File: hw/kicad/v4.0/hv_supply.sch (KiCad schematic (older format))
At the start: 32 parts, among them U4 ACT4088, U5 LNK304D

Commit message: Added LCSC # to parts in 4.3 PCB
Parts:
- C145, C35, C4, C51, C68, C69, C70, C97: LCSC (none) -> C15850
- C15, C41, C58, C60: LCSC (none) -> C14663
- C50: LCSC (none) -> C23630
- D10, D11: LCSC (none) -> C86560
- D6: LCSC (none) -> C8678
- D8: LCSC (none) -> C2297
- R143: LCSC (none) -> C22843
- R15, R16, R30, R75, R91: LCSC (none) -> C21190
- R161: LCSC (none) -> C23018
- R19, R92: LCSC (none) -> C22809
- R21: LCSC (none) -> C23196
- U4: LCSC (none) -> C11135
- U5: LCSC (none) -> C37448
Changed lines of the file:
@@
 EESchema Schematic File Version 4
 LIBS:stmbl_4.0-cache
-EELAYER 26 0
+EELAYER 30 0
 EELAYER END
 $Descr A4 11693 8268
@@
 F 9 "" H 0   0   50  0001 C CNN "Description"
 F 10 "Micro Commercial Co" H 0   0   50  0001 C CNN "Manufacturer"
+F 11 "C86560" H 6400 4250 50  0001 C CNN "LCSC"
 	1    6400 4250
 	0    1    1    0
@@
 F 9 "" H 0   0   50  0001 C CNN "Description"
 F 10 "Micro Commercial Co" H 0   0   50  0001 C CNN "Manufacturer"
+F 11 "C86560" H 7200 3750 50  0001 C CNN "LCSC"
 	1    7200 3750
 	0    1    1    0
@@
 F 9 "" H 0   0   50  0001 C CNN "Description"
 F 10 "" H 0   0   50  0001 C CNN "Manufacturer"
+F 11 " C14663" H 7200 4250 50  0001 C CNN "LCSC"
 	1    7200 4250
 	1    0    0    -1
@@
 F 9 "" H 0   0   50  0001 C CNN "Description"
 F 10 "" H 0   0   50  0001 C CNN "Manufacturer"
+F 11 " C15850" H 6400 3750 50  0001 C CNN "LCSC"
 	1    6400 3750
 	1    0    0    -1
@@
 F 9 "" H 0   0   50  0001 C CNN "Description"
 F 10 "" H 0   0   50  0001 C CNN "Manufacturer"
+F 11 " C14663" H 5250 3750 50  0001 C CNN "LCSC"
 	1    5250 3750
 	1    0    0    -1
@@
 F 9 "" H 0   0   50  0001 C CNN "Description"
 F 10 "" H 0   0   50  0001 C CNN "Manufacturer"
+F 11 "C21190" H 5600 3750 50  0001 C CNN "LCSC"
 	1    5600 3750
 	-1   0    0    1
@@
 F 9 "" H 0   0   50  0001 C CNN "Description"
 F 10 "" H 0   0   50  0001 C CNN "Manufacturer"
+F 11 "C22809" H 6550 3100 50  0001 C CNN "LCSC"
 	1    6550 3100
 	0    -1   -1   0
@@
 F 9 "" H 0   0   50  0001 C CNN "Description"
 F 10 "Lite-On" H 0   0   50  0001 C CNN "Manufacturer"
+F 11 "C2297" H 9300 4350 50  0001 C CNN "LCSC"
 	1    9300 4350
 	0    -1   -1   0
@@
 F 9 "" H 0   0   50  0001 C CNN "Description"
 F 10 "" H 0   0   50  0001 C CNN "Manufacturer"
+F 11 "C21190" H 9300 3900 50  0001 C CNN "LCSC"
 	1    9300 3900
 	1    0    0    -1
@@
 F 9 "" H 0   0   50  0001 C CNN "Description"
 F 10 "" H 0   0   50  0001 C CNN "Manufacturer"
+F 11 "C23196" H 2700 6200 50  0001 C CNN "LCSC"
 	1    2700 6200
 	0    1    1    0
@@
 F 9 "" H 0   0   50  0001 C CNN "Description"
 F 10 "" H 0   0   50  0001 C CNN "Manufacturer"
+F 11 "C22809" H 2450 6450 50  0001 C CNN "LCSC"
 	1    2450 6450
 	1    0    0    -1
@@
 F 9 "" H 0   0   50  0001 C CNN "Description"
 F 10 "Multicomp" H 0   0   50  0001 C CNN "Manufacturer"
+F 11 "C8678" H 2950 6850 50  0001 C CNN "LCSC"
 	1    2950 6850
 	0    1    1    0
@@
 F 9 "" H 0   0   50  0001 C CNN "Description"
 F 10 "" H 0   0   50  0001 C CNN "Manufacturer"
+F 11 " C14663" H 2600 5900 50  0001 C CNN "LCSC"
 	1    2600 5900
 	0    -1   -1   0
@@
 F 9 "" H 0   0   50  0001 C CNN "Description"
 F 10 "Active-Semi" H 0   0   50  0001 C CNN "Manufacturer"
+F 11 "C11135" H 1950 6050 50  0001 C CNN "LCSC"
 	1    1950 6050
 	1    0    0    -1
@@
 F 9 "" H 0   0   50  0001 C CNN "Description"
 F 10 "" H 0   0   50  0001 C CNN "Manufacturer"
+F 11 "C21190" H 9300 3500 50  0001 C CNN "LCSC"
 	1    9300 3500
 	1    0    0    -1
@@
 F 9 "" H 0   0   50  0001 C CNN "Description"
 F 10 "" H 0   0   50  0001 C CNN "Manufacturer"
+F 11 " C15850" H 3750 6450 50  0001 C CNN "LCSC"
 	1    3750 6450
 	1    0    0    -1
@@
 F 9 "" H 0   0   50  0001 C CNN "Description"
 F 10 "" H 0   0   50  0001 C CNN "Manufacturer"
+F 11 " C14663" H 3250 6450 50  0001 C CNN "LCSC"
 	1    3250 6450
 	1    0    0    -1
@@
 F 9 "" H 0   0   50  0001 C CNN "Description"
 F 10 "Power Integrations" H 0   0   50  0001 C CNN "Manufacturer"
+F 11 "C37448" H 4600 3600 50  0001 C CNN "LCSC"
 	1    4600 3600
 	1    0    0    -1
@@
 F 9 "" H 0   0   50  0001 C CNN "Description"
 F 10 "" H 0   0   50  0001 C CNN "Manufacturer"
+F 11 "C21190" H 2450 6850 50  0001 C CNN "LCSC"
 	1    2450 6850
 	1    0    0    -1
@@
 F 9 "" H 0   0   50  0001 C CNN "Description"
 F 10 "" H 0   0   50  0001 C CNN "Manufacturer"
+F 11 "C21190" H 5600 3350 50  0001 C CNN "LCSC"
 	1    5600 3350
 	-1   0    0    1
@@
 F 9 "" H 0   0   50  0001 C CNN "Description"
 F 10 "" H 0   0   50  0001 C CNN "Manufacturer"
+F 11 "C22843" H 6150 3100 50  0001 C CNN "LCSC"
 	1    6150 3100
 	0    -1   -1   0
@@
 F 9 "" H 0   0   50  0001 C CNN "Description"
 F 10 "" H 0   0   50  0001 C CNN "Manufacturer"
+F 11 "C23630" H 3500 6450 50  0001 C CNN "LCSC"
 	1    3500 6450
 	1    0    0    -1
@@
 F 9 "" H 0   0   50  0001 C CNN "Description"
 F 10 "" H 0   0   50  0001 C CNN "Manufacturer"
+F 11 " C15850" H 7950 4250 50  0001 C CNN "LCSC"
 	1    7950 4250
 	1    0    0    -1
@@
 F 9 "" H 0   0   50  0001 C CNN "Description"
 F 10 "" H 0   0   50  0001 C CNN "Manufacturer"
+F 11 " C15850" H 7450 4250 50  0001 C CNN "LCSC"
 	1    7450 4250
 	1    0    0    -1
@@
 F 9 "" H 0   0   50  0001 C CNN "Description"
 F 10 "" H 0   0   50  0001 C CNN "Manufacturer"
+F 11 " C15850" H 4000 6450 50  0001 C CNN "LCSC"
 	1    4000 6450
 	1    0    0    -1
@@
 F 9 "" H 0   0   50  0001 C CNN "Description"
 F 10 "" H 0   0   50  0001 C CNN "Manufacturer"
+F 11 "C23018" H 8700 4250 50  0001 C CNN "LCSC"
 	1    8700 4250
 	1    0    0    -1
@@
 F 9 "" H 0   0   50  0001 C CNN "Description"
 F 10 "" H 0   0   50  0001 C CNN "Manufacturer"
+F 11 " C15850" H 7700 4250 50  0001 C CNN "LCSC"
 	1    7700 4250
 	1    0    0    -1
@@
 F 9 "" H 0   0   50  0001 C CNN "Description"
 F 10 "" H 0   0   50  0001 C CNN "Manufacturer"
+F 11 " C15850" H 8200 4250 50  0001 C CNN "LCSC"
 	1    8200 4250
 	1    0    0    -1
@@
 F 9 "" H 0   0   50  0001 C CNN "Description"
 F 10 "" H 0   0   50  0001 C CNN "Manufacturer"
+F 11 " C15850" H 8450 4250 50  0001 C CNN "LCSC"
 	1    8450 4250
 	1    0    0    -1

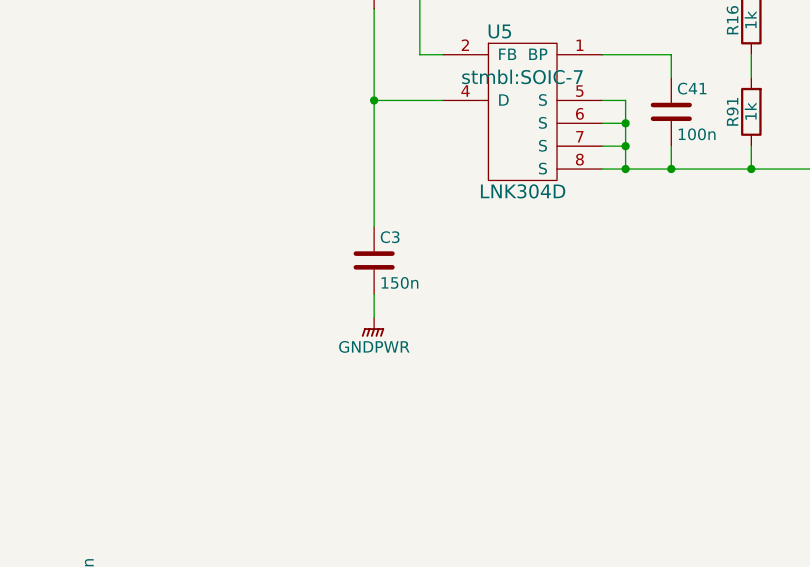
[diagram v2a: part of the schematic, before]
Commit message: Changed 120uf 1808 to 1210 100uF
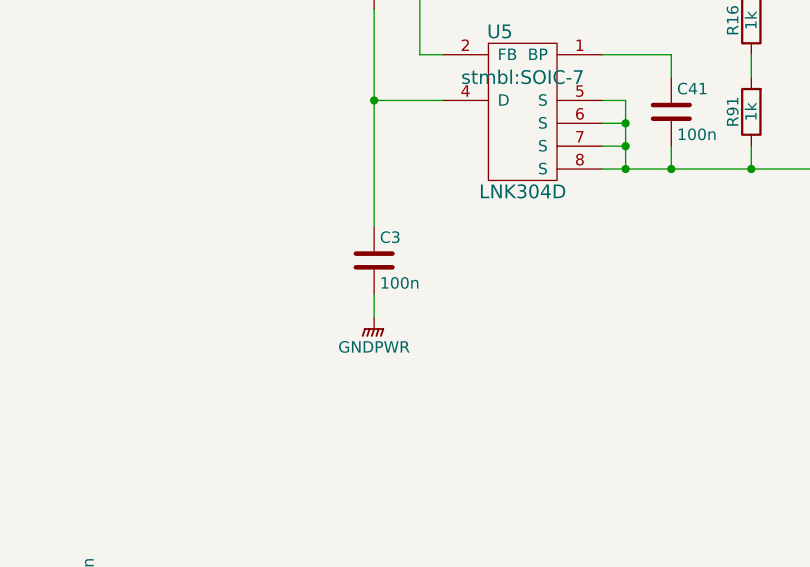
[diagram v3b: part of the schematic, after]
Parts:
- C145, C35, C4, C51, C68, C69, C70, C97: LCSC C15850 -> C15850
- C15, C41, C58, C60: LCSC C14663 -> C14663
- C3: value 150n -> 100n; footprint stmbl:C_1808 -> Capacitor_SMD:C_1210_3225Metric; LCSC (none) -> C141218; Manufacturer No C1808W154KCRACTU -> C1210C104KCRAC7800
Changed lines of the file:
@@
 F 9 "" H 0   0   50  0001 C CNN "Description"
 F 10 "" H 0   0   50  0001 C CNN "Manufacturer"
-F 11 " C14663" H 7200 4250 50  0001 C CNN "LCSC"
+F 11 "C14663" H 7200 4250 50  0001 C CNN "LCSC"
 	1    7200 4250
 	1    0    0    -1
@@
 F 9 "" H 0   0   50  0001 C CNN "Description"
 F 10 "" H 0   0   50  0001 C CNN "Manufacturer"
-F 11 " C15850" H 6400 3750 50  0001 C CNN "LCSC"
+F 11 "C15850" H 6400 3750 50  0001 C CNN "LCSC"
 	1    6400 3750
 	1    0    0    -1
@@
 F 9 "" H 0   0   50  0001 C CNN "Description"
 F 10 "" H 0   0   50  0001 C CNN "Manufacturer"
-F 11 " C14663" H 5250 3750 50  0001 C CNN "LCSC"
+F 11 "C14663" H 5250 3750 50  0001 C CNN "LCSC"
 	1    5250 3750
 	1    0    0    -1
@@
 F 9 "" H 0   0   50  0001 C CNN "Description"
 F 10 "" H 0   0   50  0001 C CNN "Manufacturer"
-F 11 " C14663" H 2600 5900 50  0001 C CNN "LCSC"
+F 11 "C14663" H 2600 5900 50  0001 C CNN "LCSC"
 	1    2600 5900
 	0    -1   -1   0
@@
 F 9 "" H 0   0   50  0001 C CNN "Description"
 F 10 "" H 0   0   50  0001 C CNN "Manufacturer"
-F 11 " C15850" H 3750 6450 50  0001 C CNN "LCSC"
+F 11 "C15850" H 3750 6450 50  0001 C CNN "LCSC"
 	1    3750 6450
 	1    0    0    -1
@@
 F 9 "" H 0   0   50  0001 C CNN "Description"
 F 10 "" H 0   0   50  0001 C CNN "Manufacturer"
-F 11 " C14663" H 3250 6450 50  0001 C CNN "LCSC"
+F 11 "C14663" H 3250 6450 50  0001 C CNN "LCSC"
 	1    3250 6450
 	1    0    0    -1
@@
 P 3950 4400
 F 0 "C3" H 3975 4500 50  0000 L CNN
-F 1 "150n" H 3975 4300 50  0000 L CNN
-F 2 "stmbl:C_1808" H 3988 4250 30  0001 C CNN
+F 1 "100n" H 3975 4300 50  0000 L CNN
+F 2 "Capacitor_SMD:C_1210_3225Metric" H 3988 4250 30  0001 C CNN
 F 3 "" H 3950 4400 60  0000 C CNN
 F 4 "" H 3950 4400 60  0001 C CNN "InternalName"
-F 5 "C1808W154KCRACTU" H 3950 4400 60  0001 C CNN "Manufacturer No"
+F 5 "C1210C104KCRAC7800" H 3950 4400 60  0001 C CNN "Manufacturer No"
 F 6 "500V" H 3950 4400 60  0001 C CNN "Voltage"
 F 7 "" H 3950 4400 60  0001 C CNN "Source"
@@
 F 9 "" H 0   0   50  0001 C CNN "Description"
 F 10 "KEMET" H 0   0   50  0001 C CNN "Manufacturer"
+F 11 "C141218" H 3950 4400 50  0001 C CNN "LCSC"
 	1    3950 4400
 	1    0    0    -1
@@
 F 9 "" H 0   0   50  0001 C CNN "Description"
 F 10 "" H 0   0   50  0001 C CNN "Manufacturer"
-F 11 " C15850" H 7950 4250 50  0001 C CNN "LCSC"
+F 11 "C15850" H 7950 4250 50  0001 C CNN "LCSC"
 	1    7950 4250
 	1    0    0    -1
@@
 F 9 "" H 0   0   50  0001 C CNN "Description"
 F 10 "" H 0   0   50  0001 C CNN "Manufacturer"
-F 11 " C15850" H 7450 4250 50  0001 C CNN "LCSC"
+F 11 "C15850" H 7450 4250 50  0001 C CNN "LCSC"
 	1    7450 4250
 	1    0    0    -1
@@
 F 9 "" H 0   0   50  0001 C CNN "Description"
 F 10 "" H 0   0   50  0001 C CNN "Manufacturer"
-F 11 " C15850" H 4000 6450 50  0001 C CNN "LCSC"
+F 11 "C15850" H 4000 6450 50  0001 C CNN "LCSC"
 	1    4000 6450
 	1    0    0    -1
@@
 F 9 "" H 0   0   50  0001 C CNN "Description"
 F 10 "" H 0   0   50  0001 C CNN "Manufacturer"
-F 11 " C15850" H 7700 4250 50  0001 C CNN "LCSC"
+F 11 "C15850" H 7700 4250 50  0001 C CNN "LCSC"
 	1    7700 4250
 	1    0    0    -1
@@
 F 9 "" H 0   0   50  0001 C CNN "Description"
 F 10 "" H 0   0   50  0001 C CNN "Manufacturer"
-F 11 " C15850" H 8200 4250 50  0001 C CNN "LCSC"
+F 11 "C15850" H 8200 4250 50  0001 C CNN "LCSC"
 	1    8200 4250
 	1    0    0    -1
@@
 F 9 "" H 0   0   50  0001 C CNN "Description"
 F 10 "" H 0   0   50  0001 C CNN "Manufacturer"
-F 11 " C15850" H 8450 4250 50  0001 C CNN "LCSC"
+F 11 "C15850" H 8450 4250 50  0001 C CNN "LCSC"
 	1    8450 4250
 	1    0    0    -1

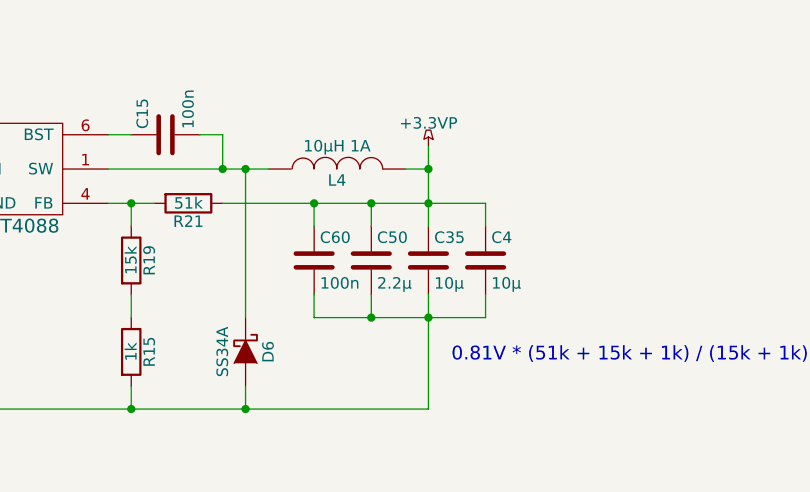
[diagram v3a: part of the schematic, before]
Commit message: Switch some 2.2uf 0603 to 1uf bypass to get 50V version on jlcpcb
Change 2.2uf 0603 to 0805 on iram to get 50V version on jlcpcb
other cleanup
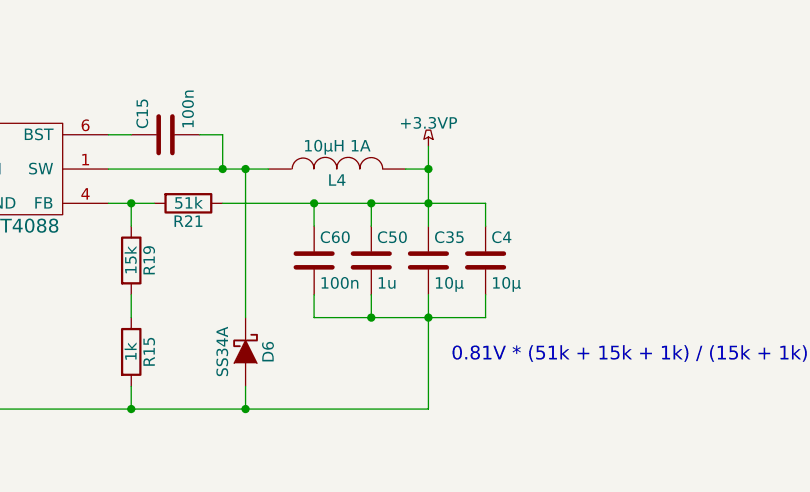
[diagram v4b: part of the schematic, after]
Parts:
- C145, C35, C4, C51, C68, C69, C70, C97: Manufacturer (none) -> Samsung Electro-Mechanics; Manufacturer No (none) -> CL21A106KAYNNNE
- C15, C41, C58, C60: Manufacturer (none) -> YAGEO; Manufacturer No (none) -> CC0603KRX7R9BB104
- C50: value 2.2µ -> 1u; LCSC C23630 -> C15849; Manufacturer (none) -> Samsung Electro-Mechanics; Manufacturer No (none) -> CL10A105KB8NNNC
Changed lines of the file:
@@
 F 4 "50V" H 7200 4250 60  0001 C CNN "Voltage"
 F 5 "" H 7200 4250 60  0001 C CNN "InternalName"
-F 6 "" H 7200 4250 60  0001 C CNN "Manufacturer No"
+F 6 "CC0603KRX7R9BB104 " H 7200 4250 60  0001 C CNN "Manufacturer No"
 F 7 "" H 7200 4250 60  0001 C CNN "Source"
 F 8 "X5R" H 7200 4250 60  0001 C CNN "Tolerance"
 F 9 "" H 0   0   50  0001 C CNN "Description"
-F 10 "" H 0   0   50  0001 C CNN "Manufacturer"
+F 10 "YAGEO" H 0   0   50  0001 C CNN "Manufacturer"
 F 11 "C14663" H 7200 4250 50  0001 C CNN "LCSC"
 	1    7200 4250
@@
 F 4 "25V" H 6400 3750 60  0001 C CNN "Voltage"
 F 5 "" H 6400 3750 60  0001 C CNN "InternalName"
-F 6 "" H 6400 3750 60  0001 C CNN "Manufacturer No"
+F 6 "CL21A106KAYNNNE" H 6400 3750 60  0001 C CNN "Manufacturer No"
 F 7 "" H 6400 3750 60  0001 C CNN "Source"
 F 8 "X5R" H 6400 3750 60  0001 C CNN "Tolerance"
 F 9 "" H 0   0   50  0001 C CNN "Description"
-F 10 "" H 0   0   50  0001 C CNN "Manufacturer"
+F 10 "Samsung Electro-Mechanics" H 0   0   50  0001 C CNN "Manufacturer"
 F 11 "C15850" H 6400 3750 50  0001 C CNN "LCSC"
 	1    6400 3750
@@
 F 4 "50V" H 5250 3750 60  0001 C CNN "Voltage"
 F 5 "" H 5250 3750 60  0001 C CNN "InternalName"
-F 6 "" H 5250 3750 60  0001 C CNN "Manufacturer No"
+F 6 "CC0603KRX7R9BB104 " H 5250 3750 60  0001 C CNN "Manufacturer No"
 F 7 "" H 5250 3750 60  0001 C CNN "Source"
 F 8 "X5R" H 5250 3750 60  0001 C CNN "Tolerance"
 F 9 "" H 0   0   50  0001 C CNN "Description"
-F 10 "" H 0   0   50  0001 C CNN "Manufacturer"
+F 10 "YAGEO" H 0   0   50  0001 C CNN "Manufacturer"
 F 11 "C14663" H 5250 3750 50  0001 C CNN "LCSC"
 	1    5250 3750
@@
 F 3 "" H 2600 5900 60  0000 C CNN
 F 4 "" H 2600 5900 60  0001 C CNN "InternalName"
-F 5 "" H 2600 5900 60  0001 C CNN "Manufacturer No"
+F 5 "CC0603KRX7R9BB104 " H 2600 5900 60  0001 C CNN "Manufacturer No"
 F 6 "50V" H 2600 5900 60  0001 C CNN "Voltage"
 F 7 "" H 2600 5900 60  0001 C CNN "Source"
 F 8 "X5R" H 2600 5900 60  0001 C CNN "Tolerance"
 F 9 "" H 0   0   50  0001 C CNN "Description"
-F 10 "" H 0   0   50  0001 C CNN "Manufacturer"
+F 10 "YAGEO" H 0   0   50  0001 C CNN "Manufacturer"
 F 11 "C14663" H 2600 5900 50  0001 C CNN "LCSC"
 	1    2600 5900
@@
 F 4 "25V" H 3750 6450 60  0001 C CNN "Voltage"
 F 5 "" H 3750 6450 60  0001 C CNN "InternalName"
-F 6 "" H 3750 6450 60  0001 C CNN "Manufacturer No"
+F 6 "CL21A106KAYNNNE" H 3750 6450 60  0001 C CNN "Manufacturer No"
 F 7 "" H 3750 6450 60  0001 C CNN "Source"
 F 8 "X5R" H 3750 6450 60  0001 C CNN "Tolerance"
 F 9 "" H 0   0   50  0001 C CNN "Description"
-F 10 "" H 0   0   50  0001 C CNN "Manufacturer"
+F 10 "Samsung Electro-Mechanics" H 0   0   50  0001 C CNN "Manufacturer"
 F 11 "C15850" H 3750 6450 50  0001 C CNN "LCSC"
 	1    3750 6450
@@
 F 3 "" H 3250 6450 60  0000 C CNN
 F 4 "" H 3250 6450 60  0001 C CNN "InternalName"
-F 5 "" H 3250 6450 60  0001 C CNN "Manufacturer No"
+F 5 "CC0603KRX7R9BB104 " H 3250 6450 60  0001 C CNN "Manufacturer No"
 F 6 "50V" H 3250 6450 60  0001 C CNN "Voltage"
 F 7 "" H 3250 6450 60  0001 C CNN "Source"
 F 8 "X5R" H 3250 6450 60  0001 C CNN "Tolerance"
 F 9 "" H 0   0   50  0001 C CNN "Description"
-F 10 "" H 0   0   50  0001 C CNN "Manufacturer"
+F 10 "YAGEO" H 0   0   50  0001 C CNN "Manufacturer"
 F 11 "C14663" H 3250 6450 50  0001 C CNN "LCSC"
 	1    3250 6450
@@
 P 3500 6450
 F 0 "C50" H 3525 6550 50  0000 L CNN
-F 1 "2.2µ" H 3525 6350 50  0000 L CNN
+F 1 "1u" H 3525 6350 50  0000 L CNN
 F 2 "stmbl:C_0603" H 3538 6300 30  0001 C CNN
 F 3 "" H 3500 6450 60  0000 C CNN
 F 4 "35V" H 3500 6450 60  0001 C CNN "Voltage"
 F 5 "" H 3500 6450 60  0001 C CNN "InternalName"
-F 6 "" H 3500 6450 60  0001 C CNN "Manufacturer No"
+F 6 "CL10A105KB8NNNC" H 3500 6450 60  0001 C CNN "Manufacturer No"
 F 7 "" H 3500 6450 60  0001 C CNN "Source"
 F 8 "X5R" H 3500 6450 60  0001 C CNN "Tolerance"
 F 9 "" H 0   0   50  0001 C CNN "Description"
-F 10 "" H 0   0   50  0001 C CNN "Manufacturer"
-F 11 "C23630" H 3500 6450 50  0001 C CNN "LCSC"
+F 10 "Samsung Electro-Mechanics" H 0   0   50  0001 C CNN "Manufacturer"
+F 11 "C15849" H 3500 6450 50  0001 C CNN "LCSC"
 	1    3500 6450
 	1    0    0    -1
@@
 F 4 "25V" H 7950 4250 60  0001 C CNN "Voltage"
 F 5 "" H 7950 4250 60  0001 C CNN "InternalName"
-F 6 "" H 7950 4250 60  0001 C CNN "Manufacturer No"
+F 6 "CL21A106KAYNNNE" H 7950 4250 60  0001 C CNN "Manufacturer No"
 F 7 "" H 7950 4250 60  0001 C CNN "Source"
 F 8 "X5R" H 7950 4250 60  0001 C CNN "Tolerance"
 F 9 "" H 0   0   50  0001 C CNN "Description"
-F 10 "" H 0   0   50  0001 C CNN "Manufacturer"
+F 10 "Samsung Electro-Mechanics" H 0   0   50  0001 C CNN "Manufacturer"
 F 11 "C15850" H 7950 4250 50  0001 C CNN "LCSC"
 	1    7950 4250
@@
 F 4 "25V" H 7450 4250 60  0001 C CNN "Voltage"
 F 5 "" H 7450 4250 60  0001 C CNN "InternalName"
-F 6 "" H 7450 4250 60  0001 C CNN "Manufacturer No"
+F 6 "CL21A106KAYNNNE" H 7450 4250 60  0001 C CNN "Manufacturer No"
 F 7 "" H 7450 4250 60  0001 C CNN "Source"
 F 8 "X5R" H 7450 4250 60  0001 C CNN "Tolerance"
 F 9 "" H 0   0   50  0001 C CNN "Description"
-F 10 "" H 0   0   50  0001 C CNN "Manufacturer"
+F 10 "Samsung Electro-Mechanics" H 0   0   50  0001 C CNN "Manufacturer"
 F 11 "C15850" H 7450 4250 50  0001 C CNN "LCSC"
 	1    7450 4250
@@
 F 4 "25V" H 4000 6450 60  0001 C CNN "Voltage"
 F 5 "" H 4000 6450 60  0001 C CNN "InternalName"
-F 6 "" H 4000 6450 60  0001 C CNN "Manufacturer No"
+F 6 "CL21A106KAYNNNE" H 4000 6450 60  0001 C CNN "Manufacturer No"
 F 7 "" H 4000 6450 60  0001 C CNN "Source"
 F 8 "X5R" H 4000 6450 60  0001 C CNN "Tolerance"
 F 9 "" H 0   0   50  0001 C CNN "Description"
-F 10 "" H 0   0   50  0001 C CNN "Manufacturer"
+F 10 "Samsung Electro-Mechanics" H 0   0   50  0001 C CNN "Manufacturer"
 F 11 "C15850" H 4000 6450 50  0001 C CNN "LCSC"
 	1    4000 6450
@@
 F 4 "25V" H 7700 4250 60  0001 C CNN "Voltage"
 F 5 "" H 7700 4250 60  0001 C CNN "InternalName"
-F 6 "" H 7700 4250 60  0001 C CNN "Manufacturer No"
+F 6 "CL21A106KAYNNNE" H 7700 4250 60  0001 C CNN "Manufacturer No"
 F 7 "" H 7700 4250 60  0001 C CNN "Source"
 F 8 "X5R" H 7700 4250 60  0001 C CNN "Tolerance"
 F 9 "" H 0   0   50  0001 C CNN "Description"
-F 10 "" H 0   0   50  0001 C CNN "Manufacturer"
+F 10 "Samsung Electro-Mechanics" H 0   0   50  0001 C CNN "Manufacturer"
 F 11 "C15850" H 7700 4250 50  0001 C CNN "LCSC"
 	1    7700 4250
@@
 F 4 "25V" H 8200 4250 60  0001 C CNN "Voltage"
 F 5 "" H 8200 4250 60  0001 C CNN "InternalName"
-F 6 "" H 8200 4250 60  0001 C CNN "Manufacturer No"
+F 6 "CL21A106KAYNNNE" H 8200 4250 60  0001 C CNN "Manufacturer No"
 F 7 "" H 8200 4250 60  0001 C CNN "Source"
 F 8 "X5R" H 8200 4250 60  0001 C CNN "Tolerance"
 F 9 "" H 0   0   50  0001 C CNN "Description"
-F 10 "" H 0   0   50  0001 C CNN "Manufacturer"
+F 10 "Samsung Electro-Mechanics" H 0   0   50  0001 C CNN "Manufacturer"
 F 11 "C15850" H 8200 4250 50  0001 C CNN "LCSC"
 	1    8200 4250
@@
 F 4 "25V" H 8450 4250 60  0001 C CNN "Voltage"
 F 5 "" H 8450 4250 60  0001 C CNN "InternalName"
-F 6 "" H 8450 4250 60  0001 C CNN "Manufacturer No"
+F 6 "CL21A106KAYNNNE" H 8450 4250 60  0001 C CNN "Manufacturer No"
 F 7 "" H 8450 4250 60  0001 C CNN "Source"
 F 8 "X5R" H 8450 4250 60  0001 C CNN "Tolerance"
 F 9 "" H 0   0   50  0001 C CNN "Description"
-F 10 "" H 0   0   50  0001 C CNN "Manufacturer"
+F 10 "Samsung Electro-Mechanics" H 0   0   50  0001 C CNN "Manufacturer"
 F 11 "C15850" H 8450 4250 50  0001 C CNN "LCSC"
 	1    8450 4250
